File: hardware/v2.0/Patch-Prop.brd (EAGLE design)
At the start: 50 x 28 mm, 51 parts, among them IC1 TPS77033, IC2 XBEE, IC3 MMA8452Q, IC4 ATMEGA168, IC5 MCP1253, IC6 W2RV005RM, U2 MCP73831, X1 USBSMD

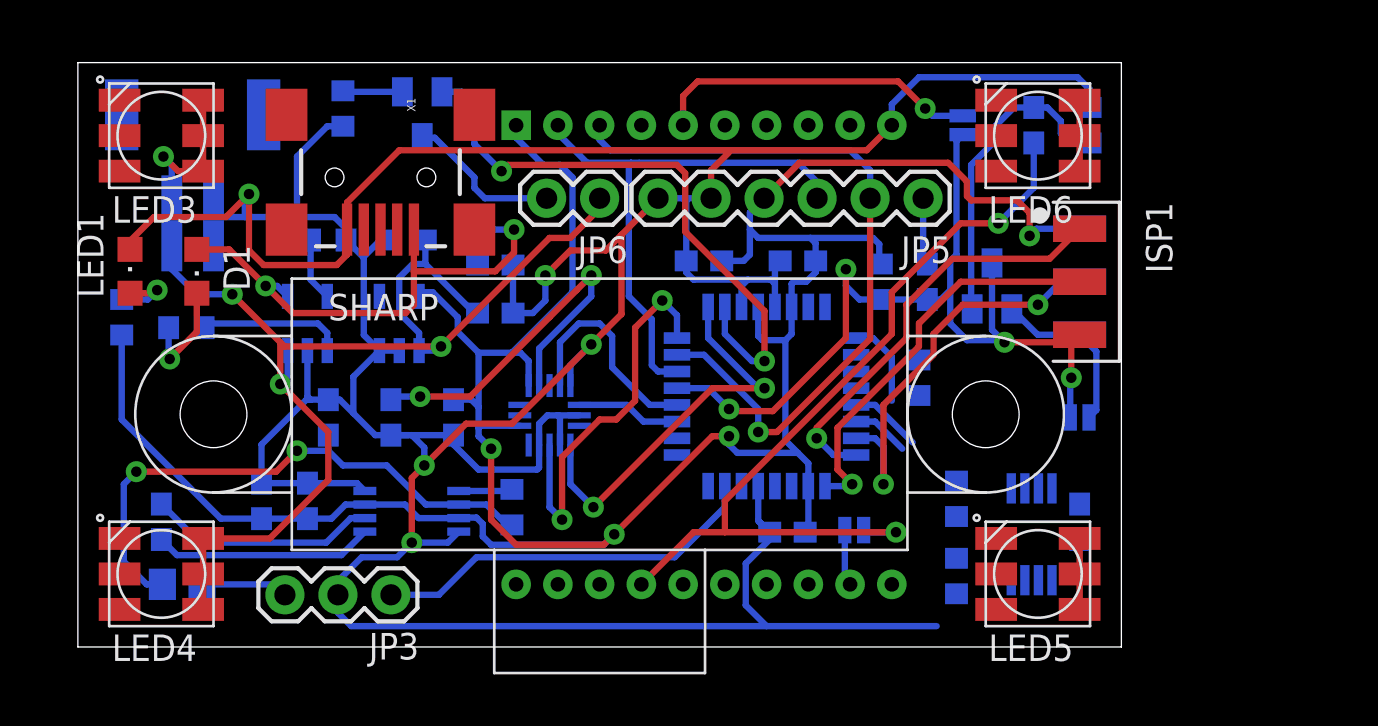
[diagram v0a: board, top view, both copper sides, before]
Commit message: Moved uC now routing LEDs
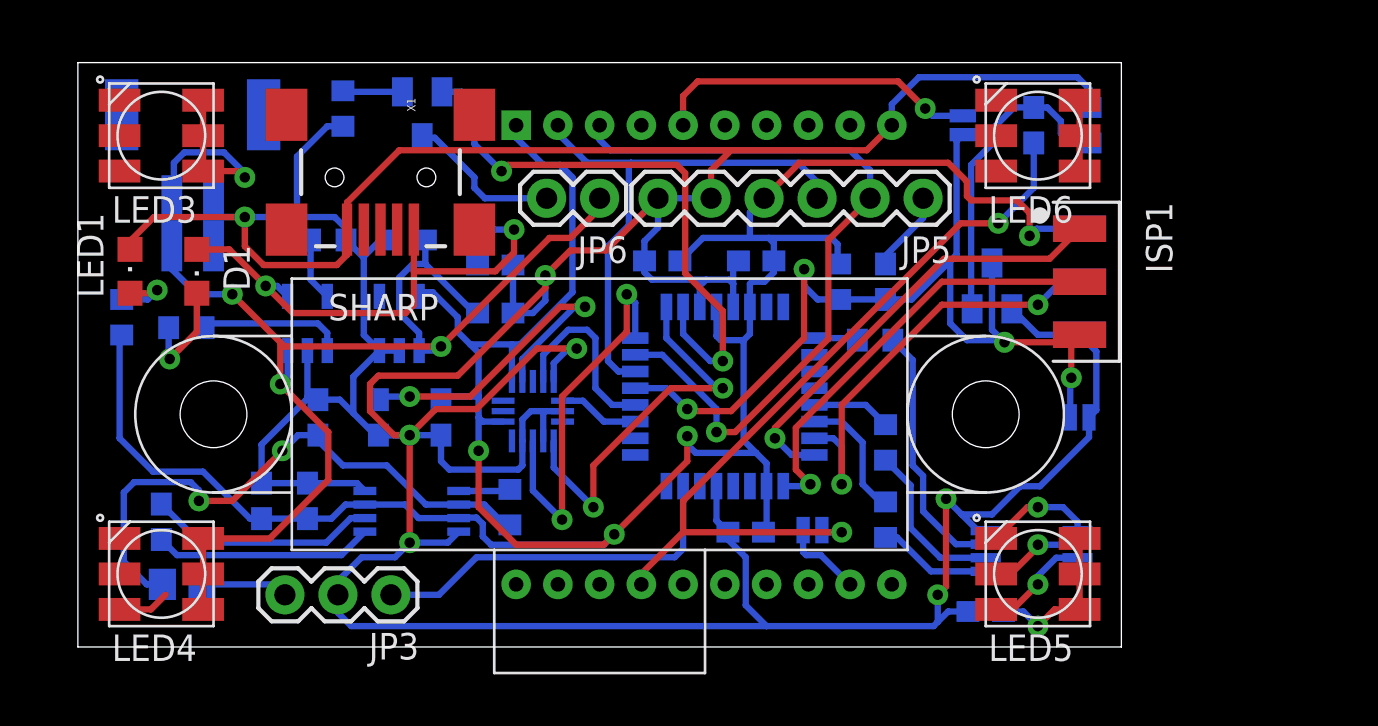
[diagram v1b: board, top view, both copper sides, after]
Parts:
- moved C7 6.22 mm to (43.5, 1.70), turned to 0 degrees
- moved R10 4.34 mm to (38.7, 9.80), turned to 90 degrees
- moved R8 4.34 mm to (38.7, 6.10), turned to 90 degrees
- moved R9 2.77 mm to (38.2, 14.7), turned to 0 degrees
- moved C12 2.00 mm to (38.7, 17.5)
- moved C13 2.00 mm to (32.0, 5.50)
- moved C14 2.00 mm to (32.5, 18.5)
- moved C9 2.00 mm to (28.0, 18.5)
- moved IC4 2.00 mm to (31.0, 12.0)
- moved R7 2.00 mm to (36.5, 17.5)
- moved SJ2 2.00 mm to (35.2, 5.60)
- moved IC3 0.82 mm to (21.8, 11.3)
- moved IC6 0.80 mm to (45.7, 4.60), turned to 180 degrees
- moved C11 0.60 mm to (17.4, 11.0)
- moved C10 0.60 mm to (14.4, 11.0)
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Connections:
- net GREEN: now also IC4.9, R9.2; no longer IC4.13, R10.2
- net GREEN_OUT: now also IC6.7; no longer IC6.6
- net RED: now also IC4.13, R10.2; no longer IC4.9, R9.2
- net RED_OUT: now also IC6.6; no longer IC6.7
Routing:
- net GND: track 222.8 -> 246.8 mm, vias 5 -> 7
- net N$12: track 0.00 -> 12.5 mm
- net V+: track 74.5 -> 82.5 mm, vias 4 -> 5
- net N$9: track 0.00 -> 7.94 mm
- net GREEN_OUT: track 0.00 -> 7.93 mm, vias 0 -> 1
- net N$7: track 0.00 -> 5.47 mm
- net BLUE_OUT: track 0.00 -> 5.24 mm, vias 0 -> 1
- net RED_OUT: track 0.00 -> 4.55 mm, vias 0 -> 1
- net BLUE: track 2.75 -> 6.17 mm
- net RESET: track 43.8 -> 46.3 mm
- net N$1: track 40.7 -> 38.6 mm
- net +3V3: track 131.6 -> 130.0 mm
- net N$18: track 2.70 -> 4.30 mm
- net N$16: track 18.4 -> 16.9 mm
- net SCL: track 10.5 -> 9.08 mm
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
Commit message: Working on LED routing, remove Xbee reset
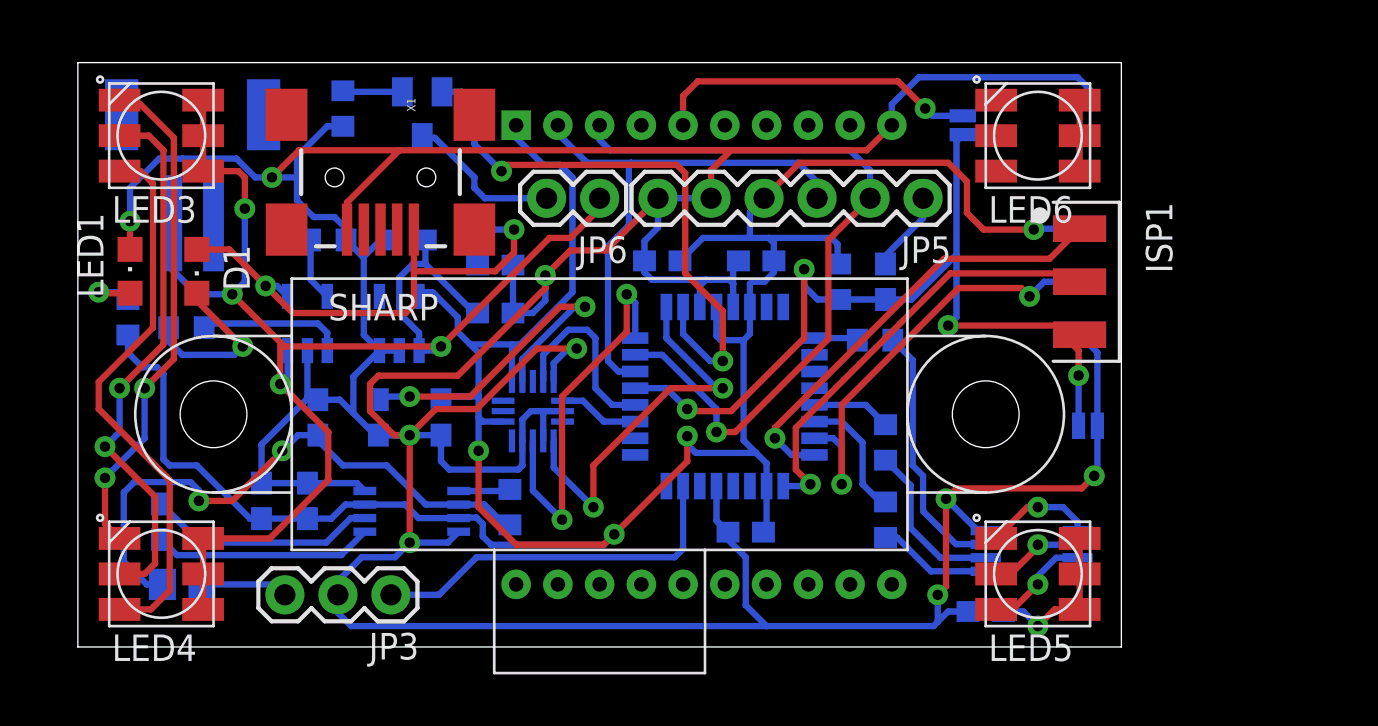
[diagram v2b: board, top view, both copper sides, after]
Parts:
- removed C6: .1uF, rcl:C0603
- removed R3: 10k, rcl:R0603
- removed SJ2: SOLDERJUMPERNO, SparkFun:SJ_2S-NO
- removed T1: (no value), transistor:SOT23-EBC
- moved SJ3 0.57 mm to (48.4, 10.6)
- moved R5 0.30 mm to (2.40, 15.8)
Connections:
- removed net N$1: C6.1, IC2.17, SJ2.2
- removed net N$18: IC2.12, SJ2.1
- removed net N$2: C6.2, R3.2, T1.B
- net GND: no longer R3.1, T1.E
- net RESET: no longer T1.C
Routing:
- net N$1: track 38.6 -> 0.00 mm, vias 2 -> 0
- net RED_OUT: track 4.55 -> 30.8 mm, vias 1 -> 3
- net BLUE_OUT: track 5.24 -> 29.4 mm, vias 1 -> 3
- net GREEN_OUT: track 7.93 -> 32.0 mm
- net N$2: track 15.2 -> 0.00 mm
- net N$18: track 4.30 -> 0.00 mm
- net N$8: track 5.21 -> 8.10 mm
- net RESET: track 46.3 -> 43.7 mm
- net MOSI: track 20.9 -> 22.1 mm
- net V+: track 82.5 -> 81.4 mm
- net +3V3: track 130.0 -> 129.2 mm
- net GND: track 246.8 -> 247.1 mm, vias 7 -> 9

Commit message: Tweaking route style and doing cleanup
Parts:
- removed D1: (no value), led:CHIPLED_0805
- added MOCW: (no value), led:CHIPLED_0805
- moved SJ1 0.90 mm to (41.5, 25.0)
- moved LED1 0.54 mm to (2.30, 18.5)
- moved C7 0.50 mm to (43.5, 2.20)
- moved C1 0.50 mm to (4.00, 6.50)
- moved C10 0.50 mm to (14.4, 11.5)
- moved C11 0.50 mm to (17.4, 11.5)
- moved C12 0.50 mm to (38.7, 18.0)
- moved C13 0.50 mm to (32.0, 6.00)
- moved C14 0.50 mm to (32.5, 19.0)
- moved C15 0.50 mm to (15.8, 20.0)
- moved C16 0.50 mm to (20.0, 18.8)
- moved C2 0.50 mm to (8.80, 7.50)
- moved C3 0.50 mm to (20.0, 16.5)
- moved C4 0.50 mm to (11.0, 7.50)
- moved C5 0.50 mm to (11.5, 11.5)
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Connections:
- net N$8: now also MOCW.C; no longer D1.C
- net USB_VIN: now also MOCW.A; no longer D1.A
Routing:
- net RED_OUT: track 30.8 -> 113.9 mm, vias 3 -> 4
- net V+: track 81.4 -> 154.3 mm, vias 5 -> 9
- net GREEN_OUT: track 32.0 -> 99.9 mm, vias 1 -> 3
- net BLUE_OUT: track 29.4 -> 94.8 mm, vias 3 -> 4
- net GND: track 247.1 -> 229.3 mm, vias 9 -> 13
- net +3V3: track 129.2 -> 142.0 mm
- net INT1: track 18.9 -> 16.1 mm
- net RESET: track 43.7 -> 45.9 mm
- net N$19: track 15.8 -> 13.6 mm, vias 1 -> 0
- net VIBE_CONTROL: track 28.1 -> 26.0 mm
- net RXD: track 26.0 -> 28.0 mm
- net INT0: track 18.7 -> 17.1 mm
- net USB_VIN: track 26.2 -> 27.1 mm
- net N$10: track 28.2 -> 27.3 mm
- net PROXIN: track 17.9 -> 17.0 mm
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- added copper zone on layer 1, net GND
- added copper zone on layer 16, net GND
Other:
- board size 50 x 28 mm -> 50 x 29 mm

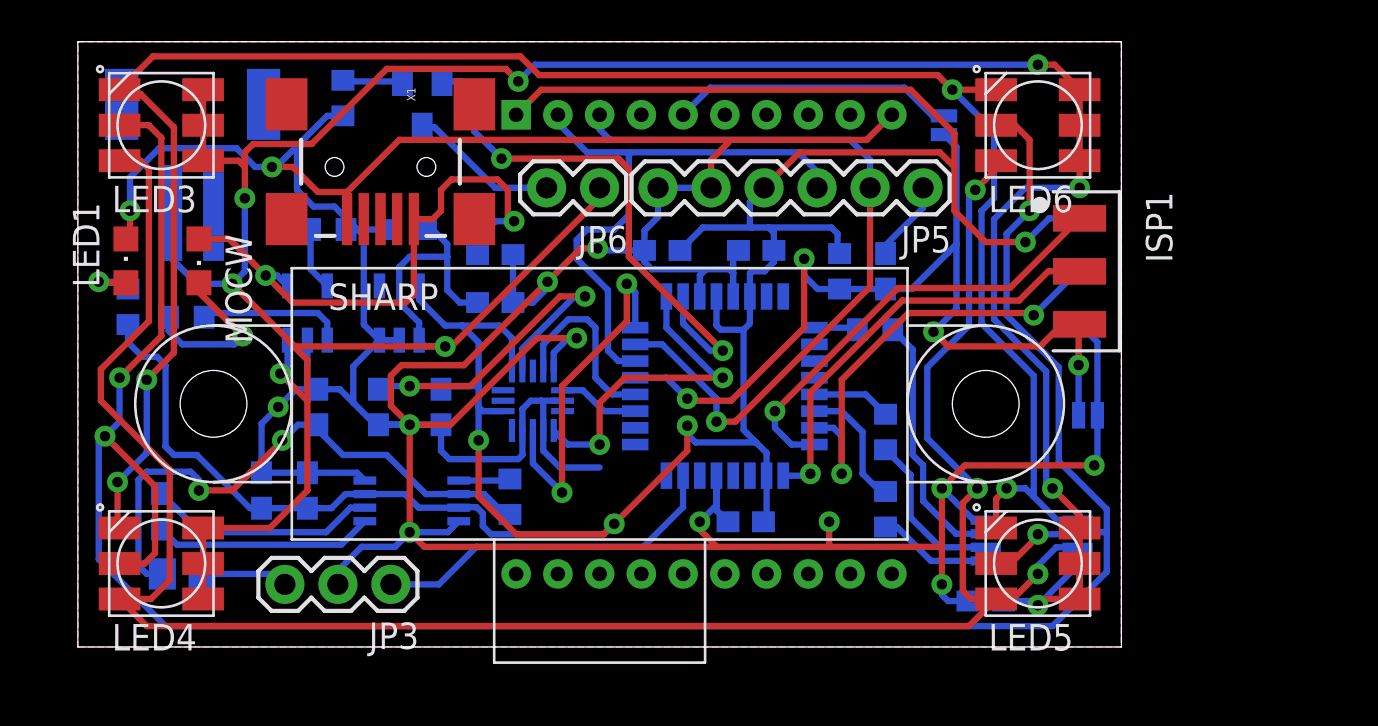
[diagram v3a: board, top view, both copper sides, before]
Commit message: Expanded board to fit mounting holes. Used extra space for breakout pins
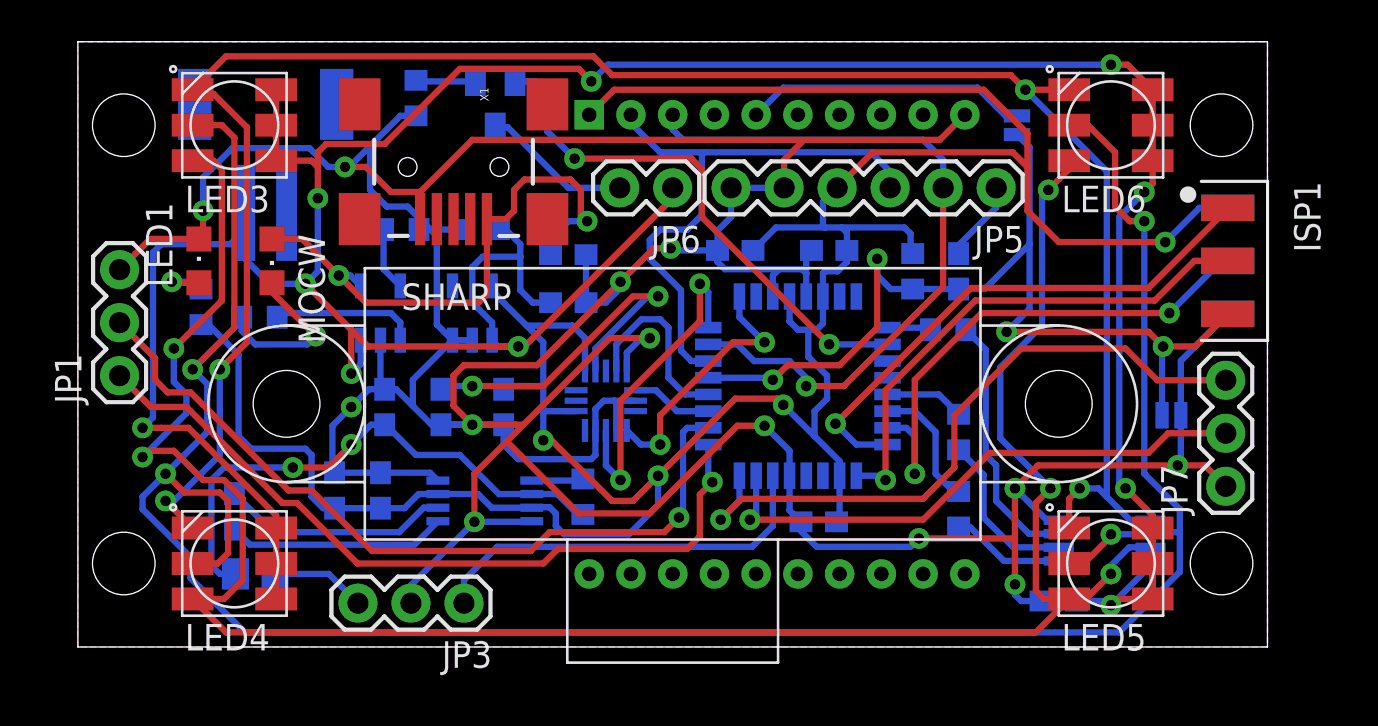
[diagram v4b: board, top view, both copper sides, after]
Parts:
- added JP1, JP7: (no value), SparkFun:1X03
- moved ISP1 7.12 mm to (55.1, 18.5)
- moved SJ3 4.00 mm to (52.4, 11.1)
- moved JP3 3.61 mm to (18.5, 2.10)
- moved MOCW 3.50 mm to (9.30, 18.5)
- moved R5 3.50 mm to (5.90, 16.3)
- moved C1 3.50 mm to (7.50, 6.50)
- moved C12 3.50 mm to (42.2, 18.0)
- moved C13 3.50 mm to (35.5, 6.00)
- moved C14 3.50 mm to (36.0, 19.0)
- moved C15 3.50 mm to (19.3, 20.0)
- moved C16 3.50 mm to (23.5, 18.8)
- moved C2 3.50 mm to (12.3, 7.50)
- moved C3 3.50 mm to (23.5, 16.5)
- moved C4 3.50 mm to (14.5, 7.50)
- moved C7 3.50 mm to (47.0, 2.20)
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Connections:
- removed net STATUS: IC4.11
- new net ADC0: IC4.23, JP7.2
- new net ADC1: IC4.24, JP7.3
- new net ADC2: IC4.25, JP1.1
- new net ADC3: IC4.26, JP1.2
- net GND: now also JP1.3, JP7.1
- net PROXIN: now also IC4.22; no longer IC4.23
- net VIBE_CONTROL: now also IC4.10; no longer IC4.2
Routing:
- net ADC3: track 0.00 -> 38.1 mm, vias 0 -> 1
- net ADC2: track 0.00 -> 36.8 mm, vias 0 -> 1
- net ADC1: track 0.00 -> 32.2 mm, vias 0 -> 1
- net ADC0: track 0.00 -> 26.7 mm, vias 0 -> 1
- net GND: track 229.3 -> 235.0 mm
- net V+: track 154.3 -> 160.1 mm, vias 9 -> 10
- net MISO: track 21.7 -> 26.0 mm
- net SCK: track 20.5 -> 24.8 mm
- net GREEN_OUT: track 99.9 -> 103.8 mm, vias 3 -> 5
- net INT1: track 16.1 -> 12.4 mm
- net MOSI: track 22.3 -> 25.1 mm
- net PROXIN: track 17.0 -> 19.4 mm
- net TXD: track 36.5 -> 34.6 mm
- net +3V3: track 142.0 -> 143.4 mm
- net INT0: track 17.1 -> 15.9 mm
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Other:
- board size 50 x 29 mm -> 57 x 29 mm

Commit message: Smashed and adjusted part names, added pin annotation
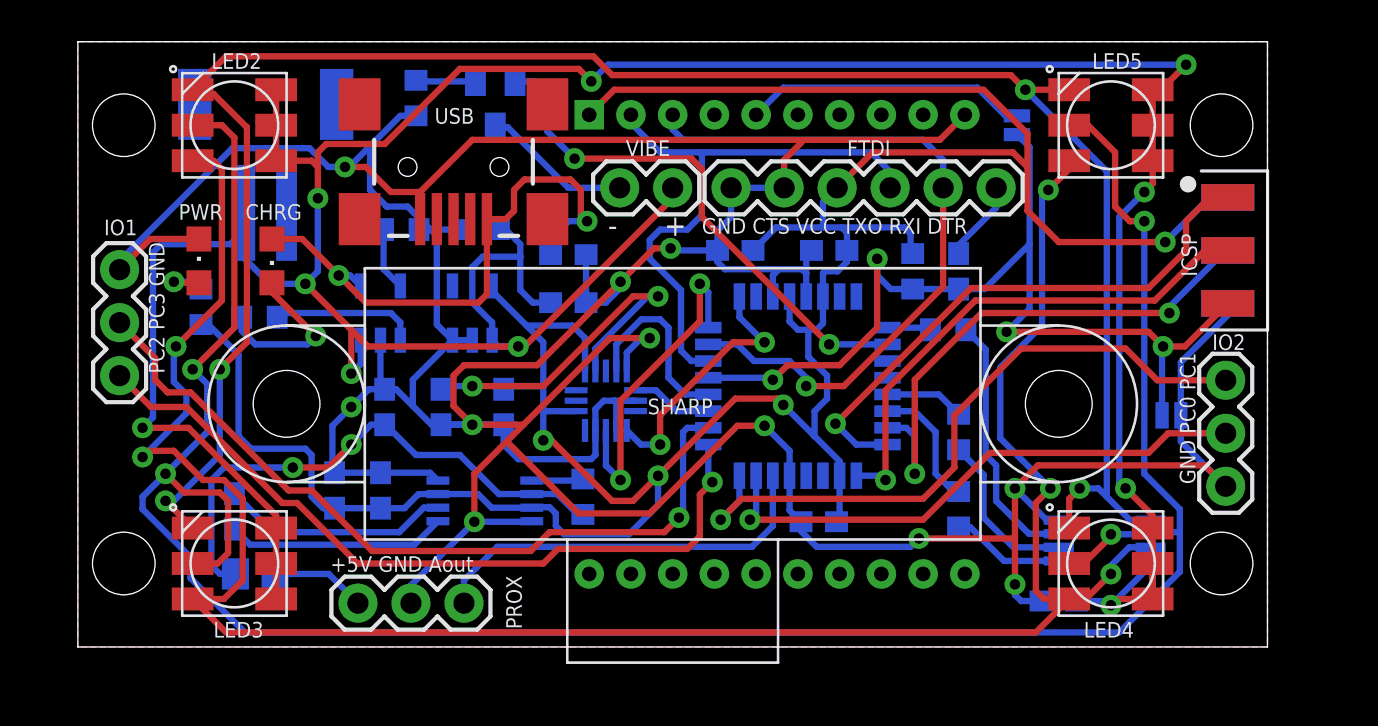
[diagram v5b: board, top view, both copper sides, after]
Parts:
- removed C15, C16: 4.7uF, rcl:C0603
- removed IC4: ATMEGA168, SparkFun:TQFP32-08
- removed ISP1: (no value), balto:2X03_BORDER
- removed LED6: RGBLED5050, adafruit:RGBLED5050
- removed R10: 4.7k, rcl:R0603
- removed SJ3: SOLDERJUMPERNO, SparkFun:SJ_2S-NO
- added C6: .1uF, rcl:C0603
- added C8: 10uF, rcl:C0603
- added ICSP: (no value), balto:2X03_BORDER
- added LED2: RGBLED5050, adafruit:RGBLED5050
- added R3: 2k, rcl:R0603
- added SJ2: SOLDERJUMPERNO, SparkFun:SJ_2S-NO
- added XBEE: XBEE, adafruit:XBEE
- C1: value 1uF -> 4.7uF
- C10: value 0.1uF -> 10uF
- C11: value 4.7uF -> 0.1uF
- C12: value .1uF -> 0.1uF
- C13: value 10uF -> 4.7uF
- C14: value .1uF -> 4.7uF
- C5: value 10uF -> .1uF
- C9: value 0.1uF -> 1uF
- IC2: value XBEE -> ATMEGA168; device adafruit:XBEE -> SparkFun:TQFP32-08
- IC3: value MMA8452Q -> MCP1253; device eski-ic:QFN-16 -> CH_Microchip:MSOP8
- IC5: value MCP1253 -> MMA8452Q; device CH_Microchip:MSOP8 -> eski-ic:QFN-16
- R1: value 100k -> RLim
- R4: value 2k -> 10k
- R6: value RLim -> 100k
- R7: value 10k -> 4.7k
- moved LED4 42.0 mm to (49.5, 4.00)
- moved C7 35.1 mm to (12.3, 7.50), turned to 90 degrees
- moved C9 27.1 mm to (7.50, 6.50), turned to 90 degrees
- moved C12 25.6 mm to (17.4, 11.5)
- moved R4 24.6 mm to (40.0, 18.0), turned to 90 degrees
- moved C5 22.6 mm to (36.0, 19.0), turned to 0 degrees
- moved C4 21.1 mm to (35.5, 6.00), turned to 0 degrees
- moved LED3 21.0 mm to (7.50, 4.00)
- moved LED5 21.0 mm to (49.5, 25.0)
- moved R1 20.7 mm to (16.2, 26.3)
- moved R6 20.7 mm to (24.2, 7.20)
- moved C1 20.2 mm to (23.5, 18.8), turned to 180 degrees
- moved C14 20.1 mm to (47.0, 2.20)
- moved C13 16.1 mm to (20.4, 11.5), turned to 270 degrees
- moved SJ1 15.7 mm to (52.4, 11.1), turned to 0 degrees
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- renumbered JP1 to IO1, JP2 to BATT, JP3 to PROX, JP5 to FTDI, JP6 to VIBE, JP7 to IO2, LED1 to PWR, MOCW to CHRG, T2 to T1, U2 to IC7, X1 to USB
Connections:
- net +3V3: now also C5.1, C7.1, C8.1, IC2.18, IC2.4, IC2.6, IC3.3, IC3.7, IC5.PIN1, IC5.PIN14, ICSP.2, R4.2, XBEE.1; no longer C14.1, C2.1, C9.1, IC2.1, IC3.PIN1, IC3.PIN14, IC4.18, IC4.4, IC4.6, IC5.3, IC5.7, ISP1.2, R7.2
- net ADC0: now also IC2.23; no longer IC4.23
- net ADC1: now also IC2.24; no longer IC4.24
- net ADC2: now also IC2.25; no longer IC4.25
- net ADC3: now also IC2.26; no longer IC4.26
- net BLUE: now also IC2.14, R7.2; no longer IC4.14, R8.2
- net BLUE_OUT: now also LED2.4; no longer LED6.4
- net DTR: now also C6.1; no longer C12.1
- net GND: now also C1.2, C12.2, C8.2, IC2.21, IC2.3, IC2.5, IC3.4, IC3.8, IC5.PIN10, IC5.PIN12, IC5.PIN5, IC5.PIN7, ICSP.6, R1.1, R3.2, SJ1.1, XBEE.10; no longer C15.2, C16.2, C9.2, IC2.10, IC3.PIN10, IC3.PIN12, IC3.PIN5, IC3.PIN7, IC4.21, IC4.3, IC4.5, IC5.4, IC5.8, ISP1.6, R4.2, R6.1, SJ3.1
- net GREEN: now also IC2.9; no longer IC4.9
- net GREEN_OUT: now also LED2.6; no longer LED6.6
- net INT0: now also IC2.32, IC5.PIN11; no longer IC3.PIN11, IC4.32
- net INT1: now also IC2.1, IC5.PIN9; no longer IC3.PIN9, IC4.1
- net MISO: now also IC2.16, ICSP.1; no longer IC4.16, ISP1.1
- net MOSI: now also IC2.15, ICSP.4; no longer IC4.15, ISP1.4
- net N$10: now also C10.1, IC3.2, R6.1; no longer C5.1, IC5.2, R1.1
- net N$11: now also R3.1; no longer R4.1
- net N$16: now also C12.1, IC5.PIN2; no longer C10.1, IC3.PIN2
- net N$19: now also SJ2.1, XBEE.5; no longer IC2.5, SJ1.1
- net N$3: now also C9.1, IC3.5; no longer C1.1, IC5.5
- net N$4: now also R1.2; no longer R6.2
- net N$6: now also C9.2, IC3.6; no longer C1.2, IC5.6
- net N$7: now also R7.1; no longer R8.1
- net N$9: now also R8.1; no longer R10.1
- net PGOOD: now also IC3.1, R6.2; no longer IC5.1, R1.2
- net PROXIN: now also IC2.22; no longer IC4.22
- net RED: now also IC2.13, R8.2; no longer IC4.13, R10.2
- net RED_OUT: now also LED2.5; no longer LED6.5
- net RESET: now also C6.2, IC2.29, ICSP.5, R4.1, SJ2.2; no longer C12.2, IC4.29, ISP1.5, R7.1, SJ3.2
- net RXD: now also IC2.30, XBEE.2; no longer IC2.2, IC4.30
- net SCK: now also IC2.17, ICSP.3; no longer IC4.17, ISP1.3
- net SCL: now also IC2.28, IC5.PIN4; no longer IC3.PIN4, IC4.28
- net SDA: now also IC2.27, IC5.PIN6; no longer IC3.PIN6, IC4.27
- net TXD: now also IC2.31, XBEE.3; no longer IC2.3, IC4.31
- net USB_VIN: now also C1.1; no longer C16.1
- net V+: now also C14.1, C2.1, LED2.1, LED2.2, LED2.3; no longer C15.1, C7.1, LED6.1, LED6.2, LED6.3
- net VIBE_CONTROL: now also IC2.10; no longer IC4.10
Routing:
- net GND: track 235.0 -> 240.7 mm, vias 13 -> 11
- net V+: track 160.1 -> 163.3 mm
- net SCK: track 24.8 -> 26.0 mm
- net MISO: track 26.0 -> 27.0 mm
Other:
- board text added: "+"
- board text added: "+5V GND Aout"
- board text added: "-"
- board text added: "GND CTS VCC TXO RXI DTR"
- board text added: "GND PC0 PC1"
- board text added: "PC2 PC3 GND"
